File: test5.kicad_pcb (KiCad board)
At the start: 2 copper layers, 135 parts, among them J1 JACK_TRS, J2 JACK_TRS, J3 Conn_01x04_Female, U1 NE5532, U10 LM386, U2 NE5532, U3 NE5532, U4 NE5532, U5 NE5532, U6 NE5532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

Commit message: start arranging components on the PCB
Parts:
- moved R3 104.3 mm to (39.9, 194.8)
- moved C20 103.2 mm to (101.3, 92.5), turned to 180 degrees
- moved R30 95.7 mm to (86.9, 92.5)
- moved R15 92.6 mm to (70.9, 73.2)
- moved C18 91.6 mm to (149.4, 159.6)
- moved C24 91.6 mm to (140.5, 205.4)
- moved C26 91.6 mm to (146.9, 205.4)
- moved C27 91.6 mm to (46.5, 226.9)
- moved C30 91.6 mm to (131.6, 240.9)
- moved C34 91.6 mm to (155.8, 240.9)
- moved C4 91.6 mm to (122.7, 173.6)
- moved R10 91.6 mm to (70.7, 213.0)
- moved R27 91.6 mm to (41.5, 209.2)
- moved R46 91.6 mm to (144.3, 159.6)
- moved R47 91.6 mm to (159.6, 159.6)
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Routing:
- net Vcc-: track 0.00 -> 244.8 mm, vias 0 -> 4
- net Vcc+: track 0.00 -> 155.1 mm, vias 0 -> 3
- net IN_RIGHT: track 0.00 -> 146.8 mm, vias 0 -> 2
- net IN_LEFT: track 0.00 -> 74.1 mm
- net Net-(C17-Pad1): track 0.00 -> 67.4 mm
- net Net-(C15-Pad2): track 0.00 -> 64.2 mm
- net Net-(C9-Pad1): track 0.00 -> 62.6 mm
- net Net-(C21-Pad2): track 0.00 -> 49.7 mm, vias 0 -> 3
- net Net-(C22-Pad2): track 0.00 -> 38.7 mm, vias 0 -> 2
- net GND: track 0.00 -> 36.7 mm
- net Net-(C21-Pad1): track 0.00 -> 28.7 mm
- net Net-(C22-Pad1): track 0.00 -> 25.2 mm
- net Net-(R44-Pad2): track 0.00 -> 24.7 mm
- net Net-(R17-Pad2): track 0.00 -> 24.0 mm
- net Net-(R41-Pad2): track 0.00 -> 21.1 mm
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
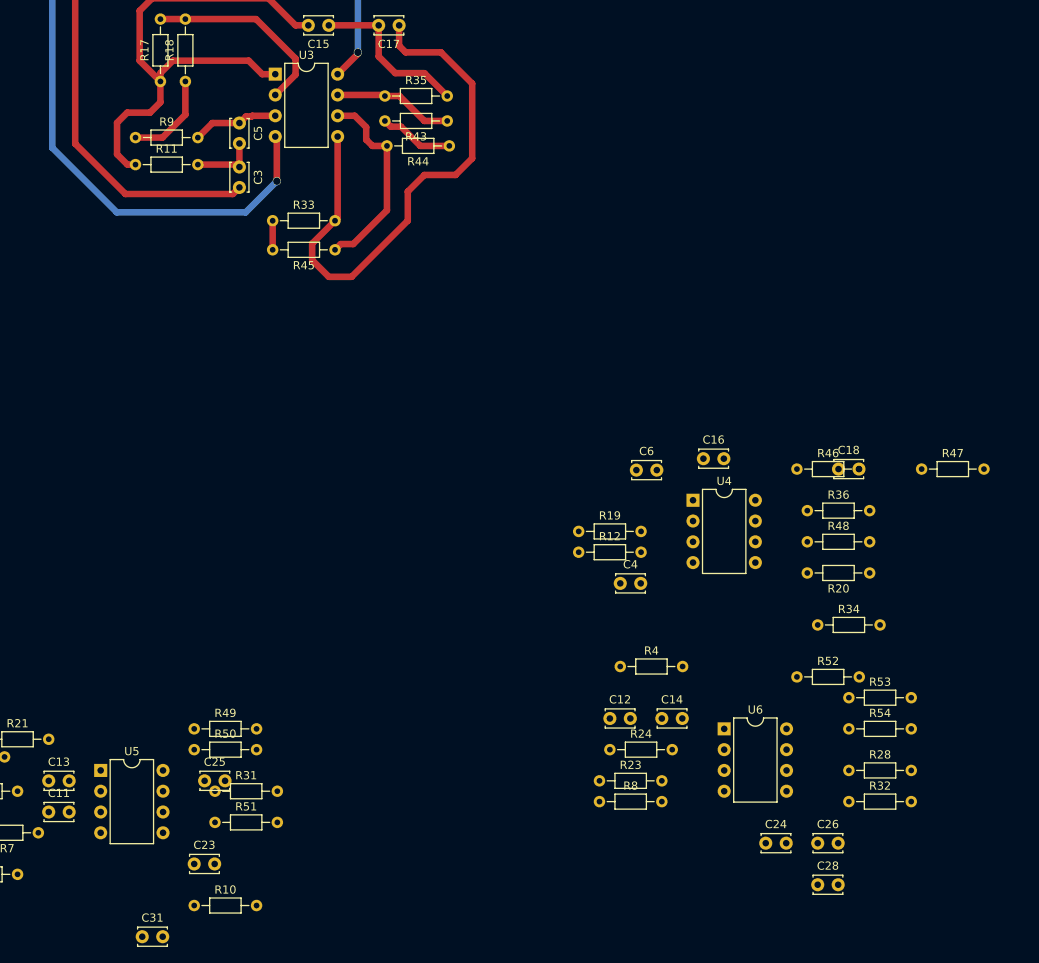
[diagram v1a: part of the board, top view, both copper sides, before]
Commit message: arrange some more components
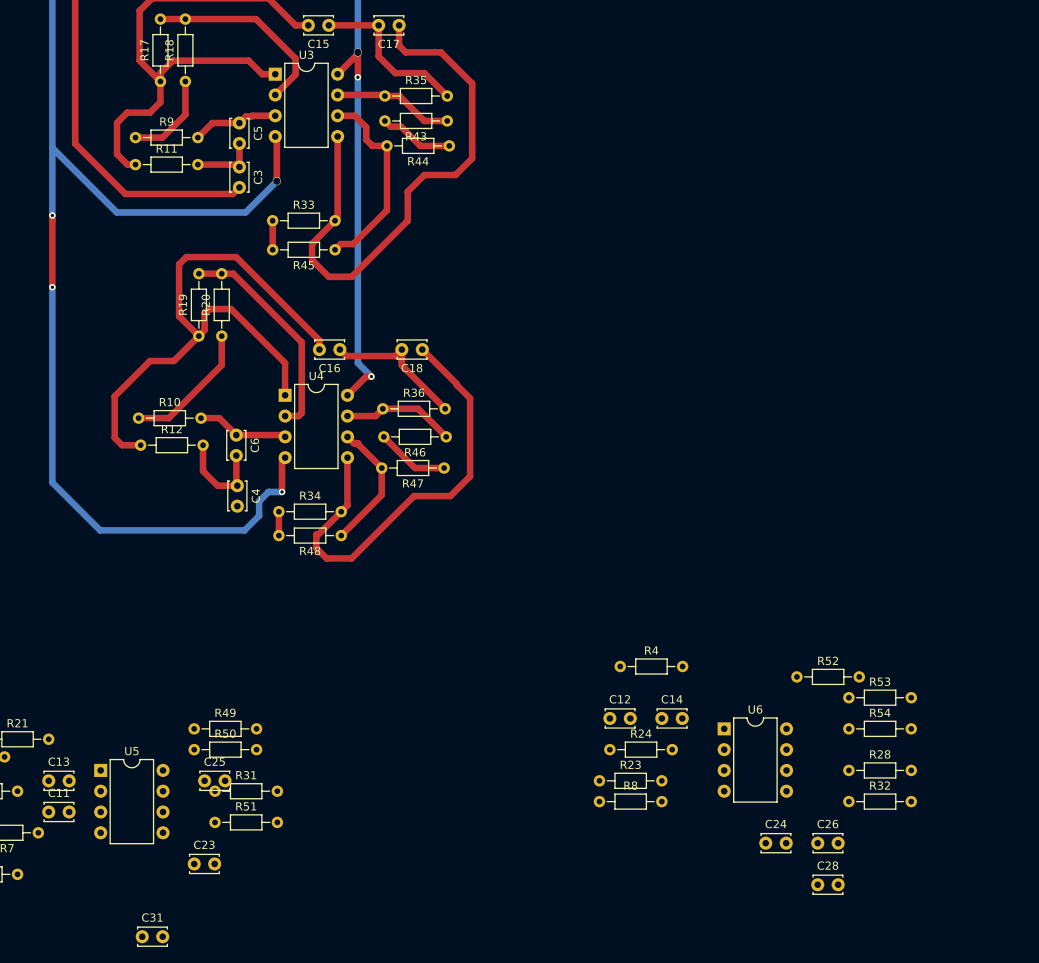
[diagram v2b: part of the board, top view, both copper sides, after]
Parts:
- moved R20 84.3 mm to (74.0, 143.4), turned to 90 degrees
- moved R34 67.3 mm to (81.0, 164.8)
- moved R10 59.9 mm to (63.9, 153.4)
- moved R47 58.4 mm to (101.2, 159.5), turned to 180 degrees
- moved R48 57.0 mm to (88.6, 167.8), turned to 180 degrees
- moved R12 55.1 mm to (64.1, 156.7)
- moved R36 53.4 mm to (93.7, 152.3)
- moved C18 52.9 mm to (98.6, 145.0), turned to 180 degrees
- moved R19 52.2 mm to (71.2, 143.4), turned to 90 degrees
- moved U4 51.5 mm to (81.8, 150.6)
- moved C6 49.1 mm to (75.8, 155.5), turned to 270 degrees
- moved C4 48.3 mm to (75.9, 161.7), turned to 270 degrees
- moved C16 46.4 mm to (88.5, 145.0), turned to 180 degrees
- moved R46 43.0 mm to (101.5, 155.7), turned to 180 degrees
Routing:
- net Vcc-: track 244.8 -> 323.6 mm, vias 4 -> 7
- net Net-(C16-Pad2): track 0.00 -> 74.4 mm
- net Net-(C18-Pad1): track 0.00 -> 54.2 mm
- net Vcc+: track 155.1 -> 199.3 mm, vias 3 -> 5
- net Net-(R19-Pad2): track 0.00 -> 26.9 mm
- net GND: track 36.7 -> 56.0 mm
- net Net-(C16-Pad1): track 0.00 -> 19.3 mm
- net Net-(R47-Pad2): track 0.00 -> 16.2 mm
- net Net-(R36-Pad1): track 0.00 -> 13.9 mm
- net Net-(C4-Pad1): track 0.00 -> 11.8 mm
- net Net-(C6-Pad1): track 0.00 -> 11.2 mm
- net Net-(R46-Pad2): track 0.00 -> 8.94 mm

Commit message: finalize layout
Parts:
- moved C35 230.3 mm to (162.8, 77.0), turned to 270 degrees
- moved RV1 229.0 mm to (122.9, 15.1), turned to 90 degrees
- moved R79 224.3 mm to (155.2, 72.9)
- moved U9 223.3 mm to (143.0, 65.3)
- moved RV2 214.2 mm to (142.2, 15.2), turned to 90 degrees
- moved R63 212.7 mm to (120.3, 32.4), turned to 90 degrees
- moved R70 210.9 mm to (122.9, 32.3), turned to 90 degrees
- moved RV4 202.9 mm to (159.3, 15.2), turned to 90 degrees
- moved R71 194.5 mm to (138.7, 31.8), turned to 90 degrees
- moved R64 192.6 mm to (141.2, 31.8), turned to 90 degrees
- moved R80 189.6 mm to (155.2, 86.9)
- moved U10 188.3 mm to (143.0, 79.2)
- moved C37 182.8 mm to (181.6, 50.3)
- moved C38 182.8 mm to (181.6, 36.3)
- moved J2 182.8 mm to (199.1, 40.1)
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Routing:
- net Net-(R69-Pad1): track 0.00 -> 331.8 mm, vias 0 -> 2
- net Vcc+: track 199.3 -> 526.8 mm, vias 5 -> 16
- net GND: track 56.0 -> 324.4 mm, vias 0 -> 14
- net Net-(R68-Pad1): track 0.00 -> 267.4 mm, vias 0 -> 2
- net Vcc-: track 323.6 -> 557.2 mm, vias 7 -> 15
- net IN_LEFT: track 74.1 -> 272.3 mm, vias 0 -> 2
- net Net-(R36-Pad1): track 13.9 -> 175.3 mm
- net Net-(R59-Pad2): track 0.00 -> 128.0 mm, vias 0 -> 2
- net Net-(R35-Pad1): track 14.7 -> 138.4 mm, vias 0 -> 2
- net Net-(RV3-Pad2): track 0.00 -> 113.8 mm, vias 0 -> 2
- net Net-(C26-Pad1): track 0.00 -> 104.2 mm
- net Net-(R63-Pad1): track 0.00 -> 103.9 mm, vias 0 -> 3
- net IN_RIGHT: track 146.8 -> 235.0 mm
- net Net-(10K1-Pad1): track 0.00 -> 85.0 mm, vias 0 -> 4
- net Net-(RV3-Pad5): track 0.00 -> 84.0 mm, vias 0 -> 2
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- added copper zone on F.Cu, net GND
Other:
- board outline added: 181.1 x 249.4 mm

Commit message: optimize layout
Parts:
- moved C12 96.7 mm to (114.8, 159.0)
- moved C24 96.7 mm to (124.8, 158.6)
- moved C25 96.7 mm to (116.8, 93.3)
- moved C26 96.7 mm to (119.1, 134.1)
- moved C32 96.7 mm to (185.2, 136.3)
- moved C34 96.7 mm to (192.2, 136.3)
- moved R21 96.7 mm to (103.4, 103.1)
- moved R23 96.7 mm to (112.8, 141.0)
- moved R24 96.7 mm to (105.2, 143.1)
- moved R28 96.7 mm to (105.2, 134.1)
- moved R4 96.7 mm to (107.2, 151.4)
- moved R52 96.7 mm to (132.6, 151.0)
- moved R53 96.7 mm to (132.5, 148.5)
- moved R54 96.7 mm to (132.5, 145.8)
- moved R69 96.7 mm to (192.0, 146.9)
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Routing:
- net Net-(R69-Pad1): track 331.8 -> 287.3 mm, vias 2 -> 4
- net IN_RIGHT: track 235.0 -> 195.6 mm
- net IN_LEFT: track 272.3 -> 238.7 mm
- net GND: track 324.4 -> 352.1 mm, vias 14 -> 20
- net Net-(R68-Pad1): track 267.4 -> 240.0 mm, vias 2 -> 4
- net Net-(C23-Pad2): track 17.1 -> 26.6 mm
- net Vcc+: track 526.8 -> 520.9 mm, vias 16 -> 14
- net Net-(R35-Pad1): track 138.4 -> 133.7 mm, vias 2 -> 4
- net Net-(C38-Pad1): track 77.4 -> 81.9 mm
- net Net-(C15-Pad1): track 20.3 -> 24.4 mm
- net Net-(C37-Pad1): track 47.0 -> 44.4 mm
- net Net-(C25-Pad2): track 67.8 -> 70.3 mm
- net Net-(R36-Pad1): track 175.3 -> 172.8 mm, vias 0 -> 2
- net Net-(C18-Pad1): track 56.1 -> 53.7 mm, vias 2 -> 0
- net Net-(C17-Pad1): track 68.1 -> 70.3 mm, vias 3 -> 0
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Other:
- board size 181.1 x 249.4 mm -> 166.1 x 165.6 mm
